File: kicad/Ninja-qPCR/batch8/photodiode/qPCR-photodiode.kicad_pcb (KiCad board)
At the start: 2 copper layers, 104.1 x 42 mm, 34 parts, among them J1 Conn_01x20_Male, J2 Conn_01x20_Male

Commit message: order batch8
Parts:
- removed D1, D10, D11, D12, D13, D14, D15, D16, D17, D2, D3, D4, D5, D6, D7, D8, D9: D_Photo, Diodes_SMD:D_1206
- removed J1, J2: Conn_01x20_Male, Pin_Headers:Pin_Header_Straight_2x10_Pitch1.27mm
- added D10A1: D_Photo, Diodes_SMD:D_1206, F.Cu at (114.6, 109.5)
- added D10B1: D_Photo, Diodes_SMD:D_1206, F.Cu at (116.6, 109.5)
- added D11A1: D_Photo, Diodes_SMD:D_1206, F.Cu at (123.6, 109.5)
- added D11B1: D_Photo, Diodes_SMD:D_1206, F.Cu at (125.6, 109.5)
- added D12A1: D_Photo, Diodes_SMD:D_1206, F.Cu at (132.6, 109.5)
- added D12B1: D_Photo, Diodes_SMD:D_1206, F.Cu at (134.6, 109.5)
- added D13A1: D_Photo, Diodes_SMD:D_1206, F.Cu at (141.6, 109.5)
- added D13B1: D_Photo, Diodes_SMD:D_1206, F.Cu at (143.6, 109.5)
- added D14A1: D_Photo, Diodes_SMD:D_1206, F.Cu at (150.6, 109.5)
- added D14B1: D_Photo, Diodes_SMD:D_1206, F.Cu at (152.6, 109.5)
- added D15A1: D_Photo, Diodes_SMD:D_1206, F.Cu at (159.6, 109.5)
- added D15B1: D_Photo, Diodes_SMD:D_1206, F.Cu at (161.6, 109.5)
- added D16A1: D_Photo, Diodes_SMD:D_1206, F.Cu at (168.6, 109.5)
- added D16B1: D_Photo, Diodes_SMD:D_1206, F.Cu at (170.6, 109.5)
- added D1A1: D_Photo, Diodes_SMD:D_1206, F.Cu at (105.6, 90.5)
- added D9A1: D_Photo, Diodes_SMD:D_1206, F.Cu at (105.6, 109.5)
- added D9B1: D_Photo, Diodes_SMD:D_1206, F.Cu at (107.6, 109.5)
- added JNA1: Conn_01x10_Male, Pin_Headers:Pin_Header_Straight_2x05_Pitch1.27mm, B.Cu at (85.8, 91.9)
- added JNB1: Conn_01x10_Male, Pin_Headers:Pin_Header_Straight_2x05_Pitch1.27mm, B.Cu at (85.8, 86.6)
- added JSA1: Conn_01x10_Male, Pin_Headers:Pin_Header_Straight_2x05_Pitch1.27mm, B.Cu at (85.8, 117.5)
- added JSB1: Conn_01x10_Male, Pin_Headers:Pin_Header_Straight_2x05_Pitch1.27mm, B.Cu at (85.8, 112.1)
- added TH1: Thermistor, Resistors_SMD:R_0603_HandSoldering, F.Cu at (90.6, 109.0)
- added TH2: Thermistor, Resistors_SMD:R_0603_HandSoldering, B.Cu at (90.6, 109.0)
- moved D1B1 11.1 mm to (107.6, 90.5)
- moved D2A1 11.1 mm to (114.6, 90.5)
- moved D2B1 11.1 mm to (116.6, 90.5)
- moved D3A1 11.1 mm to (123.6, 90.5)
- moved D3B1 11.1 mm to (125.6, 90.5)
- moved D4A1 11.1 mm to (132.6, 90.5)
- moved D4B1 11.1 mm to (134.6, 90.5)
- moved D5A1 11.1 mm to (141.6, 90.5)
- moved D5B1 11.1 mm to (143.6, 90.5)
- moved D6A1 11.1 mm to (150.6, 90.5)
- moved D6B1 11.1 mm to (152.6, 90.5)
- moved D7A1 11.1 mm to (159.6, 90.5)
- moved D7B1 11.1 mm to (161.6, 90.5)
- moved D8A1 11.1 mm to (168.6, 90.5)
- moved D8B1 11.1 mm to (170.6, 90.5)
- renumbered D18 to D1B1, D19 to D2A1, D20 to D2B1, D21 to D3A1, D22 to D3B1, D23 to D4A1, D24 to D4B1, D25 to D5A1, D26 to D5B1, D27 to D6A1, D28 to D6B1, D29 to D7A1, D30 to D7B1, D31 to D8A1, D32 to D8B1
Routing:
- net /N_PD_OUT15: track 0.00 -> 98.5 mm, vias 0 -> 2
- net /S_PD_OUT16: track 0.00 -> 94.9 mm
- net /N_PD_OUT16: track 0.00 -> 93.8 mm, vias 0 -> 2
- net /N_PD_OUT13: track 0.00 -> 90.8 mm, vias 0 -> 2
- net /S_PD_OUT15: track 0.00 -> 88.4 mm, vias 0 -> 2
- net /S_PD_OUT14: track 0.00 -> 87.1 mm
- net /N_PD_OUT14: track 0.00 -> 86.0 mm, vias 0 -> 2
- net GNDA: track 130.0 -> 213.7 mm, vias 0 -> 273
- net /N_PD_OUT11: track 0.00 -> 83.3 mm, vias 0 -> 2
- net /S_PD_OUT13: track 0.00 -> 82.1 mm, vias 0 -> 2
- net /N_PD_OUT9: track 0.00 -> 80.4 mm
- net /N_PD_OUT12: track 0.00 -> 80.0 mm, vias 0 -> 2
- net /S_PD_OUT12: track 0.00 -> 79.8 mm
- net /S_PD_OUT9: track 0.00 -> 78.0 mm, vias 0 -> 2
- net /S_PD_OUT11: track 0.00 -> 78.0 mm, vias 0 -> 2
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- added copper zone on B.Cu, net GNDA
- added copper zone on F.Cu, net GNDA
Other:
- board size 104.1 x 42 mm -> 100 x 58 mm
- board text added: "100x58mm"
- board text added: "Ninja"
- board text added: "Personal qPCR"
- board text added: "batch8/photodiode"

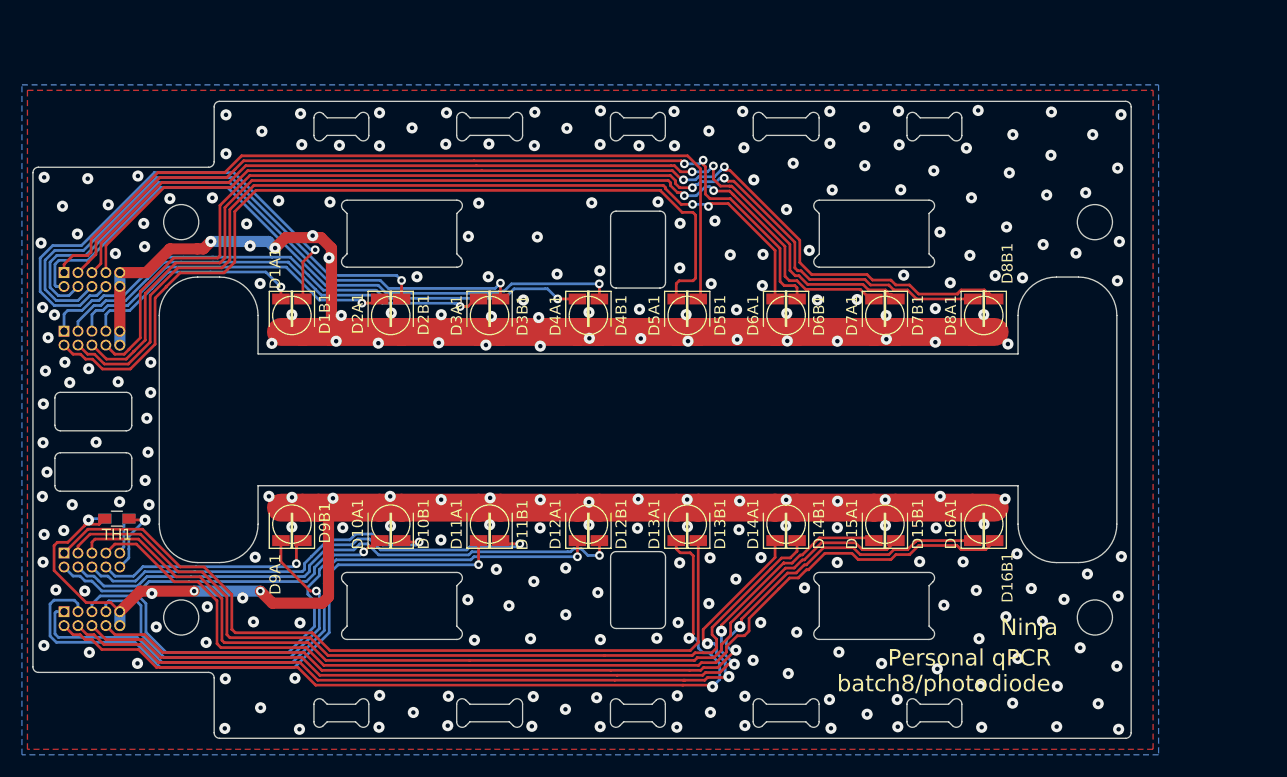
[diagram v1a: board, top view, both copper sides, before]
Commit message: ordered batch8 and got feedback
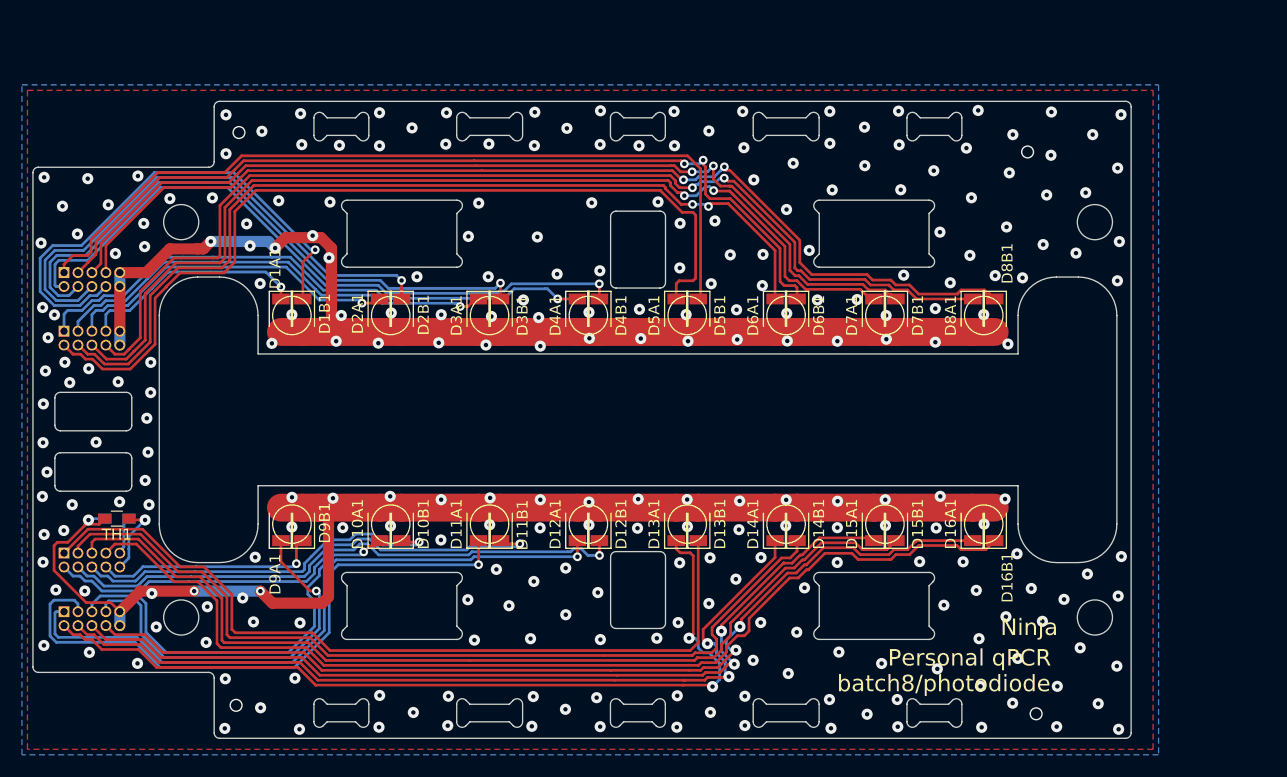
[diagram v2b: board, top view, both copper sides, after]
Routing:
- net PD_MUX_GPIO1: vias 0 -> 1
- net Net-(C13-Pad2): vias 0 -> 1
- net Net-(C11-Pad1): vias 0 -> 1
- net GNDA: vias 273 -> 272
- net /GAIN_LARGE: vias 0 -> 1

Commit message: sync
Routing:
- net GNDA: vias 272 -> 268
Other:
- outline, holes or cut-outs redrawn
